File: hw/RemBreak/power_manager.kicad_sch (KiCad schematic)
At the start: 20 parts, among them IC1 LTC2943IDD#TRPBF, J3 Screw_Terminal_01x02, J4 Conn_01x03_MountingPin, Q1 BC337, Q2 BC847, U1 INA219BxDCN, U2 MAX40200AUK

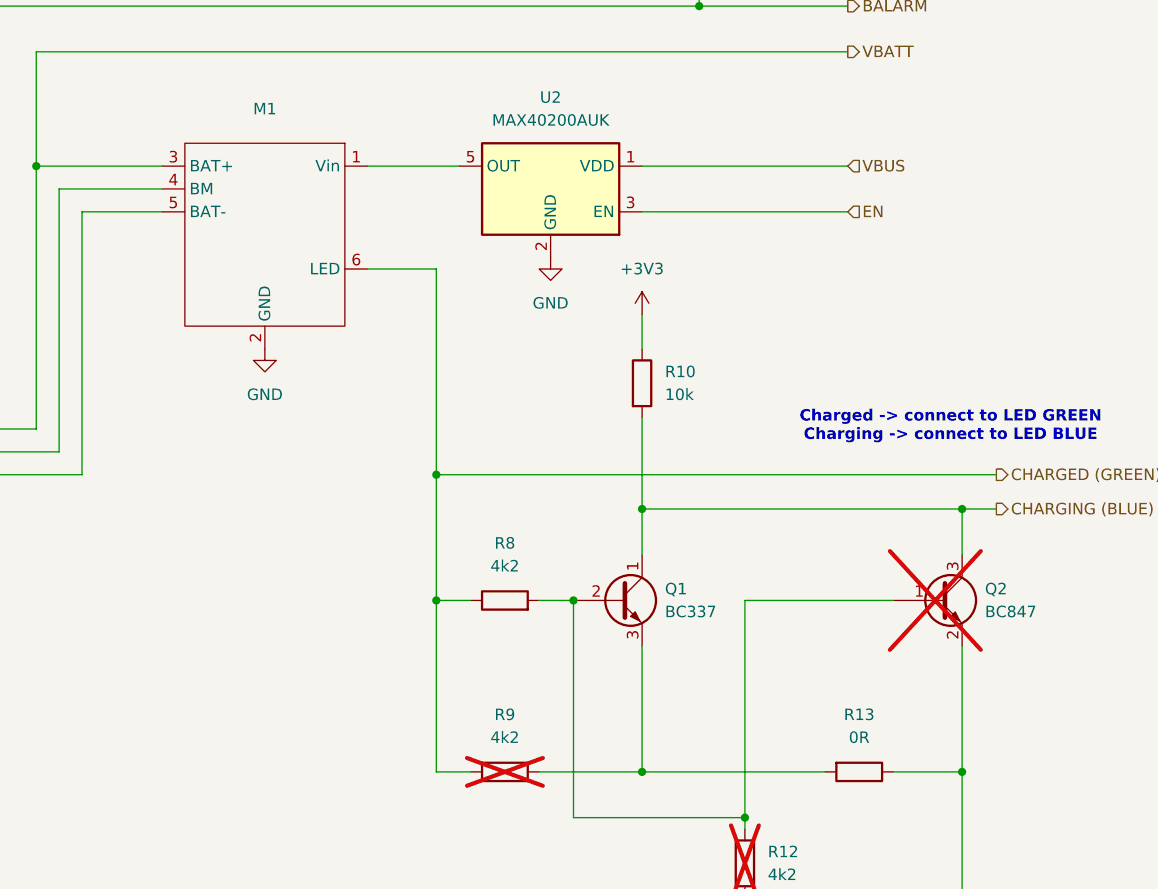
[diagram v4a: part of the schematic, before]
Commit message: updated schematics - added an extra ideal diode
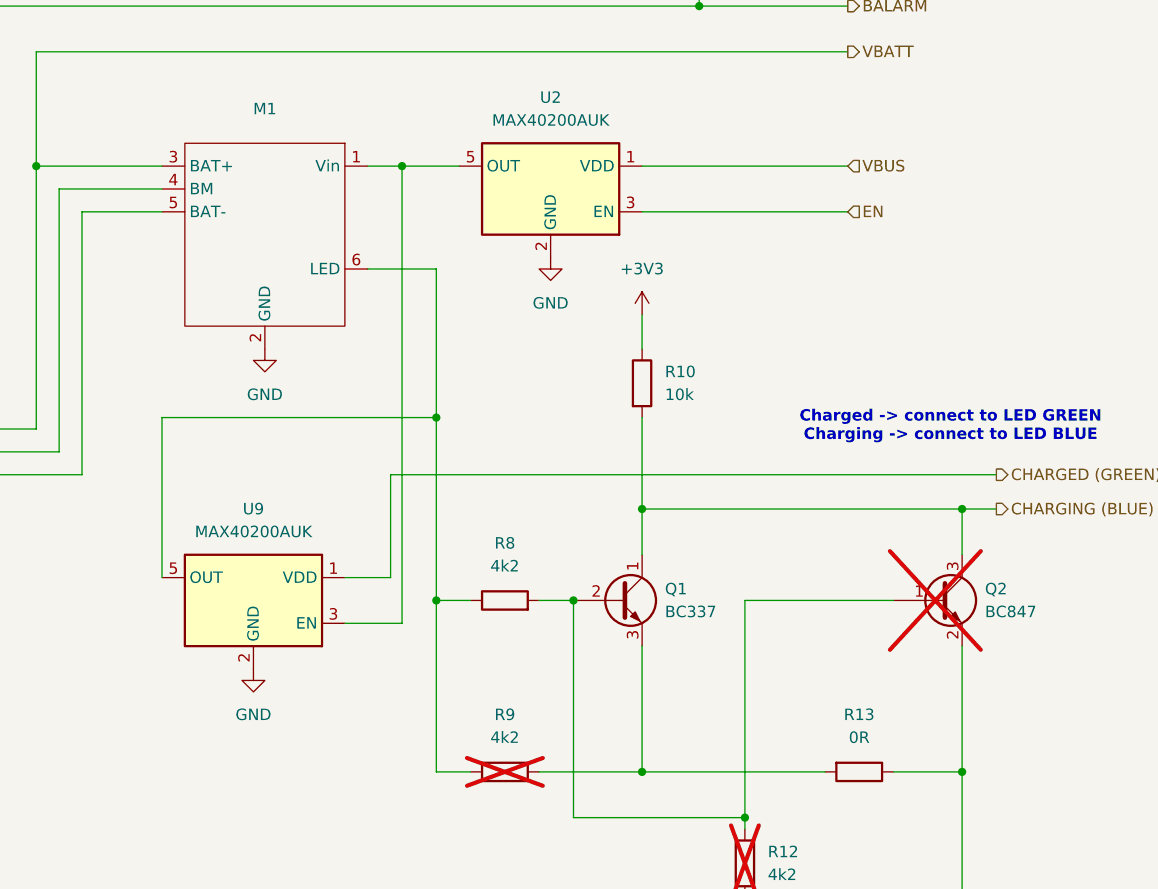
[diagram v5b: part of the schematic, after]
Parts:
- added U9: MAX40200AUK, Package_TO_SOT_SMD:SOT-23-5, symbol Analog_Switch:MAX40200AUK
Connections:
- net CHARGED (GREEN): now also U9.1 (VDD); no longer M1.6 (LED), R8.1, R9.1
- net GND: now also U9.2 (GND)
- net at M1.1 (Vin), U2.5 (OUT): now also U9.3 (EN)
- new net: M1.6 (LED), R8.1, R9.1, U9.5 (OUT)
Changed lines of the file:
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@@
 	(version 20241209)
 	(generator "eeschema")
-	(generator_version "8.99")
+	(generator_version "9.0")
 	(paper "A4")
 	(title_block
@@
 	)
 	(junction
-		(at 177.8 92.71)
-		(diameter 0)
-		(color 0 0 0 0)
-	)
-	(junction
 		(at 80.01 137.16)
 		(diameter 0)
@@
 	)
 	(junction
+		(at 173.99 58.42)
+		(diameter 0)
+		(color 0 0 0 0)
+	)
+	(junction
 		(at 34.29 77.47)
 		(diameter 0)
@@
 	)
 	(junction
+		(at 177.8 86.36)
+		(diameter 0)
+		(color 0 0 0 0)
+	)
+	(junction
 		(at 101.6 87.63)
 		(diameter 0)
@@
 	(wire
 		(pts
+			(xy 240.03 92.71) (xy 172.72 92.71)
+		)
+		(stroke
+			(width 0)
+			(type default)
+		)
+	)
+	(wire
+		(pts
 			(xy 138.43 92.71) (xy 138.43 63.5)
 		)
@@
 	(wire
 		(pts
+			(xy 173.99 109.22) (xy 173.99 58.42)
+		)
+		(stroke
+			(width 0)
+			(type default)
+		)
+	)
+	(wire
+		(pts
 			(xy 39.37 92.71) (xy 39.37 82.55)
 		)
@@
 	(wire
 		(pts
-			(xy 200.66 96.52) (xy 236.22 96.52)
+			(xy 167.64 109.22) (xy 173.99 109.22)
 		)
 		(stroke
@@
 	(wire
 		(pts
-			(xy 82.55 134.62) (xy 82.55 137.16)
+			(xy 200.66 96.52) (xy 236.22 96.52)
 		)
 		(stroke
@@
 	(wire
 		(pts
-			(xy 170.18 58.42) (xy 180.34 58.42)
+			(xy 82.55 134.62) (xy 82.55 137.16)
 		)
 		(stroke
@@
 	(wire
 		(pts
-			(xy 93.98 107.95) (xy 88.9 107.95)
+			(xy 170.18 58.42) (xy 173.99 58.42)
 		)
 		(stroke
@@
 	(wire
 		(pts
-			(xy 74.93 124.46) (xy 74.93 137.16)
+			(xy 93.98 107.95) (xy 88.9 107.95)
 		)
 		(stroke
@@
 	(wire
 		(pts
-			(xy 36.83 133.35) (xy 36.83 132.08)
+			(xy 74.93 124.46) (xy 74.93 137.16)
 		)
 		(stroke
@@
 	(wire
 		(pts
-			(xy 177.8 92.71) (xy 177.8 106.68)
+			(xy 36.83 133.35) (xy 36.83 132.08)
 		)
 		(stroke
@@
 	(wire
 		(pts
-			(xy 177.8 92.71) (xy 240.03 92.71)
-		)
-		(stroke
-			(width 0)
-			(type default)
-		)
-	)
-	(wire
-		(pts
 			(xy 34.29 87.63) (xy 66.04 87.63)
 		)
@@
 	(wire
 		(pts
+			(xy 173.99 58.42) (xy 180.34 58.42)
+		)
+		(stroke
+			(width 0)
+			(type default)
+		)
+	)
+	(wire
+		(pts
 			(xy 36.83 132.08) (xy 41.91 132.08)
 		)
@@
 	(wire
 		(pts
-			(xy 177.8 69.85) (xy 177.8 92.71)
+			(xy 177.8 69.85) (xy 177.8 86.36)
 		)
 		(stroke
@@
 	(wire
 		(pts
+			(xy 147.32 104.14) (xy 147.32 86.36)
+		)
+		(stroke
+			(width 0)
+			(type default)
+		)
+	)
+	(wire
+		(pts
 			(xy 181.61 125.73) (xy 177.8 125.73)
 		)
@@
 	(wire
 		(pts
+			(xy 172.72 92.71) (xy 172.72 104.14)
+		)
+		(stroke
+			(width 0)
+			(type default)
+		)
+	)
+	(wire
+		(pts
 			(xy 193.04 130.81) (xy 212.09 130.81)
 		)
@@
 	(wire
 		(pts
+			(xy 177.8 86.36) (xy 177.8 106.68)
+		)
+		(stroke
+			(width 0)
+			(type default)
+		)
+	)
+	(wire
+		(pts
 			(xy 34.29 87.63) (xy 34.29 77.47)
 		)
@@
 	(wire
 		(pts
+			(xy 172.72 104.14) (xy 167.64 104.14)
+		)
+		(stroke
+			(width 0)
+			(type default)
+		)
+	)
+	(wire
+		(pts
+			(xy 147.32 86.36) (xy 177.8 86.36)
+		)
+		(stroke
+			(width 0)
+			(type default)
+		)
+	)
+	(wire
+		(pts
 			(xy 39.37 92.71) (xy 39.37 95.25)
 		)
@@
 	(symbol
 		(lib_id "power:GND")
+		(at 157.48 114.3 0)
+		(unit 1)
+		(exclude_from_sim no)
+		(in_bom yes)
+		(on_board yes)
+		(dnp no)
+		(fields_autoplaced yes)
+		(property "Reference" "#PWR046"
+			(at 157.48 120.65 0)
+			(effects
+				(font
+					(size 1.27 1.27)
+				)
+				(hide yes)
+			)
+		)
+		(property "Value" "GND"
+			(at 157.48 119.38 0)
+			(effects
+				(font
+					(size 1.27 1.27)
+				)
+			)
+		)
+		(property "Footprint" ""
+			(at 157.48 114.3 0)
+			(effects
+				(font
+					(size 1.27 1.27)
+				)
+				(hide yes)
+			)
+		)
+		(property "Datasheet" ""
+			(at 157.48 114.3 0)
+			(effects
+				(font
+					(size 1.27 1.27)
+				)
+				(hide yes)
+			)
+		)
+		(property "Description" "Power symbol creates a global label with name \"GND\" , ground"
+			(at 157.48 114.3 0)
+			(effects
+				(font
+					(size 1.27 1.27)
+				)
+				(hide yes)
+			)
+		)
+		(pin "1"
+		)
+		(instances
+			(project "RemBreak"
+				(path "/e6d4ae5b-c9d7-4cbe-b288-c929fdf55a75/65dd8b54-1c0a-4683-aa46-51c439d49612"
+					(reference "#PWR046")
+					(unit 1)
+				)
+			)
+		)
+	)
+	(symbol
+		(lib_id "power:GND")
 		(at 212.09 139.7 0)
 		(unit 1)
@@
 					(unit 1)
 				)
+			)
+		)
+	)
+	(symbol
+		(lib_id "Analog_Switch:MAX40200AUK")
+		(at 157.48 106.68 0)
+		(mirror y)
+		(unit 1)
+		(exclude_from_sim no)
+		(in_bom yes)
+		(on_board yes)
+		(dnp no)
+		(property "Reference" "U9"
+			(at 157.48 96.52 0)
+			(effects
+				(font
+					(size 1.27 1.27)
+				)
+			)
+		)
+		(property "Value" "MAX40200AUK"
+			(at 157.48 99.06 0)
+			(effects
+				(font
+					(size 1.27 1.27)
+				)
+			)
+		)
+		(property "Footprint" "Package_TO_SOT_SMD:SOT-23-5"
+			(at 157.48 93.98 0)
+			(effects
+				(font
+					(size 1.27 1.27)
+				)
+				(hide yes)
+			)
+		)
+		(property "Datasheet" "https://datasheets.maximintegrated.com/en/ds/MAX40200.pdf"
+			(at 157.48 93.98 0)
+			(effects
+				(font
+					(size 1.27 1.27)
+				)
+				(hide yes)
+			)
+		)
+		(property "Description" "Ideal Diode, Ultra-Low Voltage Drop, 1.5-5.5V, 1A, SOT-23-5"
+			(at 157.48 106.68 0)
+			(effects
+				(font
+					(size 1.27 1.27)
+				)
+				(hide yes)
+			)
+		)
+		(pin "2"
+		)
+		(pin "3"
+		)
+		(pin "1"
+		)
+		(pin "5"
+		)
+		(pin "4"
+		)
+		(instances
+			(project "RemBreak"
+				(path "/e6d4ae5b-c9d7-4cbe-b288-c929fdf55a75/65dd8b54-1c0a-4683-aa46-51c439d49612"
+					(reference "U9")
+					(unit 1)
+				)

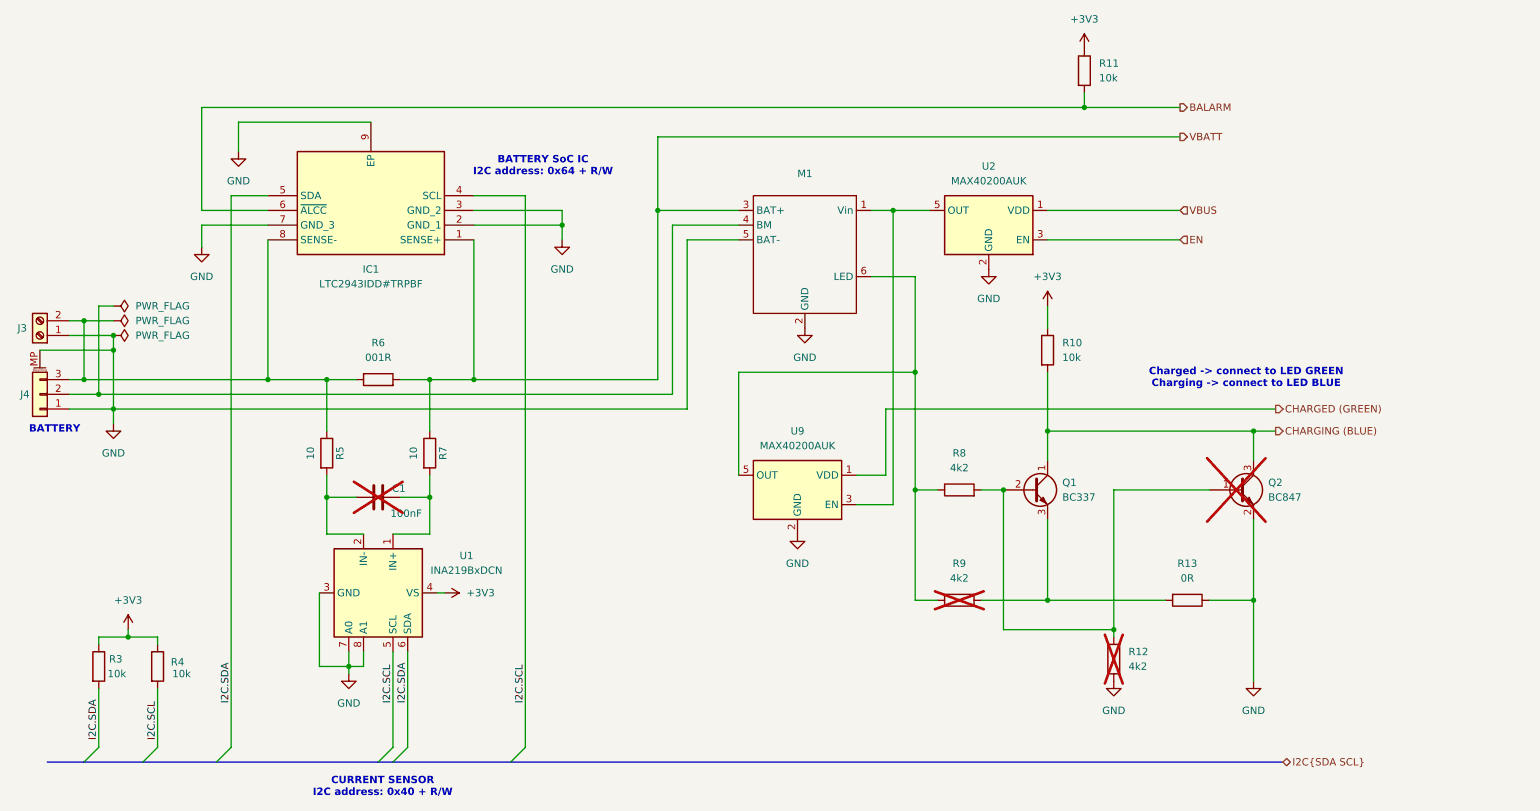
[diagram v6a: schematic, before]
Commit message: redrawing the schematics according the notes from the module design
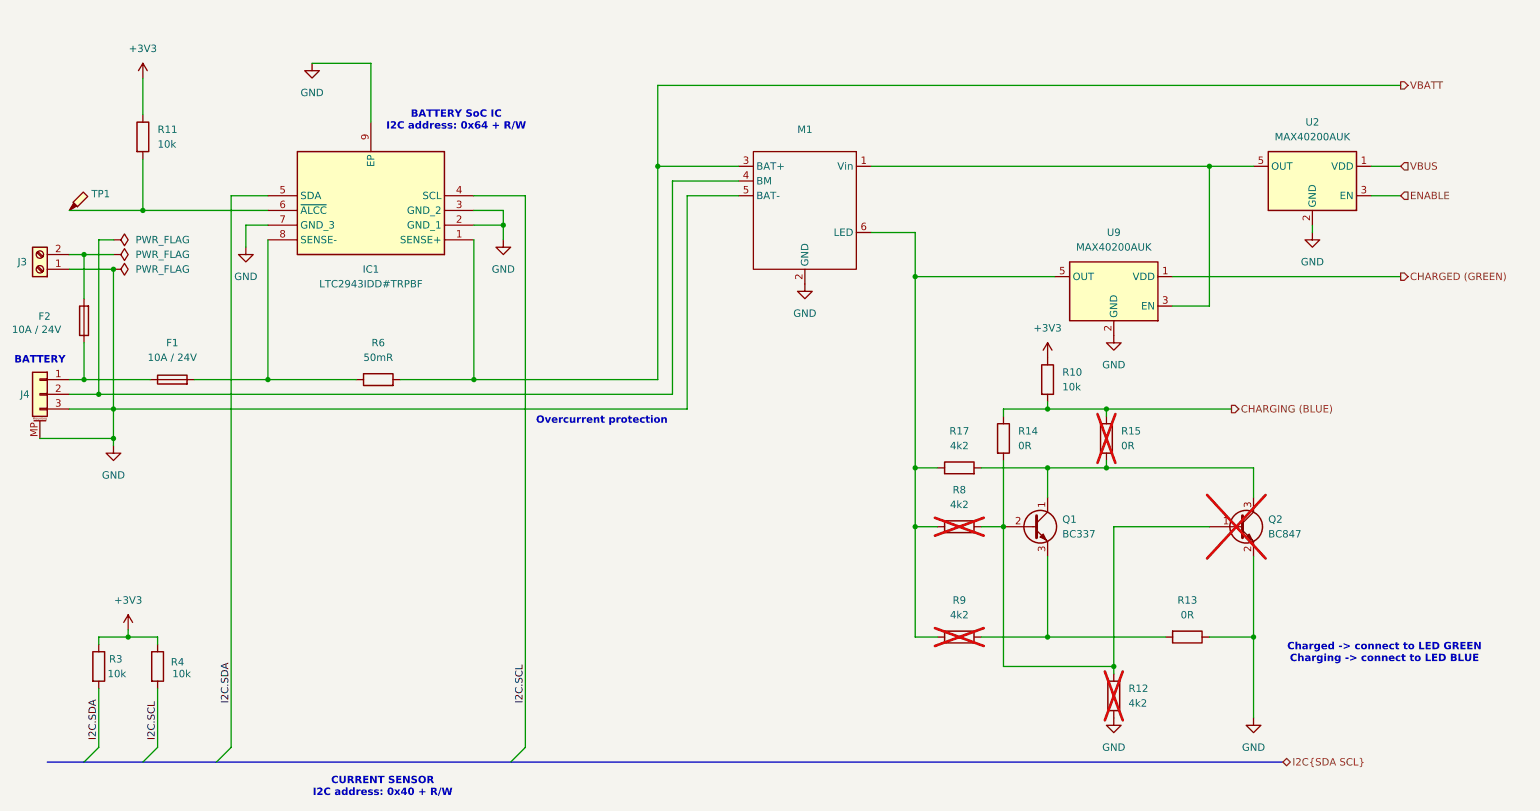
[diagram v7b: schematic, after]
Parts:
- removed C1: 100nF, Capacitor_SMD:C_0805_2012Metric_Pad1.18x1.45mm_HandSolder, symbol Device:C
- removed R5, R7: 10, Resistor_SMD:R_0805_2012Metric_Pad1.20x1.40mm_HandSolder, symbol Device:R
- removed U1: INA219BxDCN, Package_TO_SOT_SMD:SOT-23-8, symbol Sensor_Energy:INA219BxDCN
- added F1, F2: 10A / 24V, Fuse:Fuse_1206_3216Metric_Pad1.42x1.75mm_HandSolder, symbol Device:Fuse
- added R14, R15: 0R, Resistor_SMD:R_0805_2012Metric_Pad1.20x1.40mm_HandSolder, symbol Device:R
- added R17: 4k2, Resistor_SMD:R_0805_2012Metric_Pad1.20x1.40mm_HandSolder, symbol Device:R
- added TP1: TestPoint_Probe, symbol Connector:TestPoint_Probe
- R6: value 001R -> 50mR
- R8: now not fitted
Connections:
- net CHARGING (BLUE): now also R14.1, R15.1; no longer Q1.1 (C), Q2.3 (C)
- net GND: now also J4.3 (Pin_3); no longer J4.1 (Pin_1)
- net at Q1.2 (B), Q2.1 (B), R12.2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: now also R14.2
- net at IC1.8 (SENSE-), R6.1: now also F1.2; no longer J3.2 (Pin_2), J4.3 (Pin_3)
- net at M1.6 (LED), R8.1, R9.1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: now also R17.1
- net BALARM: no longer names the net of IC1.6 (~{ALCC}), R11.2
- net BALARM: now also TP1.1
- net EN renamed ENABLE
- new net: F1.1, F2.1, J4.1 (Pin_1)
- new net: F2.2, J3.2 (Pin_2)
- new net: Q1.1 (C), Q2.3 (C), R15.2, R17.2
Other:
- note added: "Overcurrent protection"
- moved on the sheet: J3, J4, M1, Q1, Q2, R10, R11, R12, R13, R9, U2, U9
